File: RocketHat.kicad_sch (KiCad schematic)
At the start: 24 parts, among them J1 Screw_Terminal_01x02, J10 Raspberry_Pi_2_3, J2 Conn_01x06_Female, J3 Conn_01x06_Female, J4 Conn_01x07_Female, J5 Conn_01x06_Female, J6 Conn_01x04_Female, J7 Conn_01x10_Female, J9 Conn_01x10_Female, Q1 FQP27P06, U1 CAT24C128

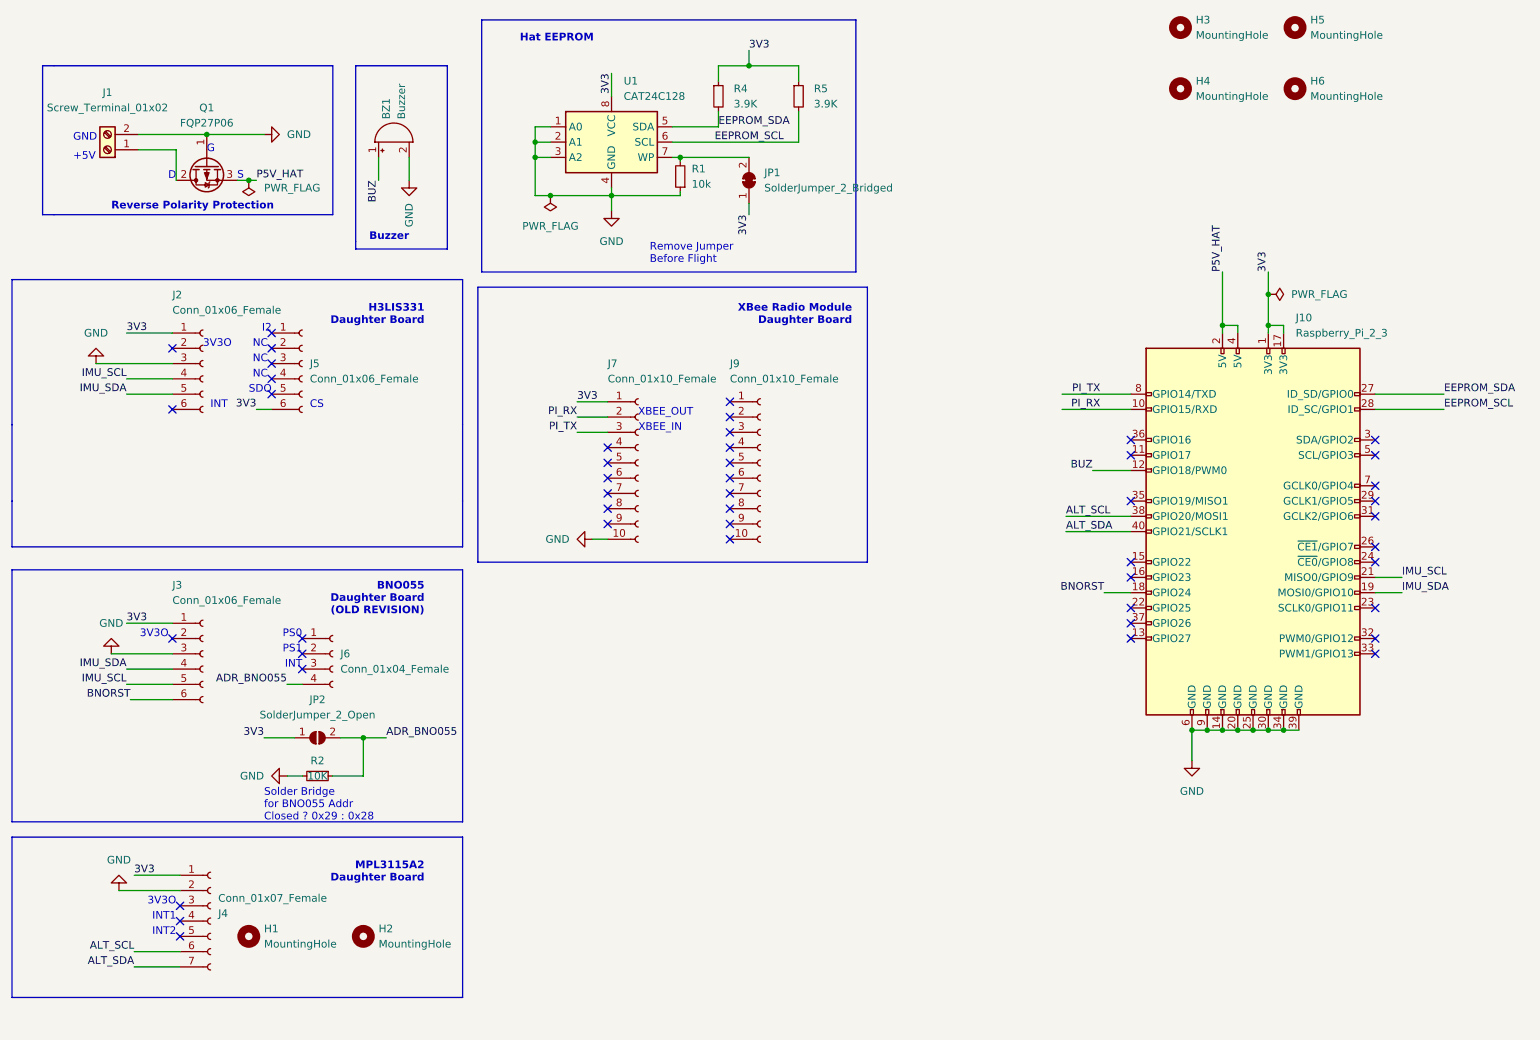
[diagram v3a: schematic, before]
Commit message: Added Mounting Holes for all sensors
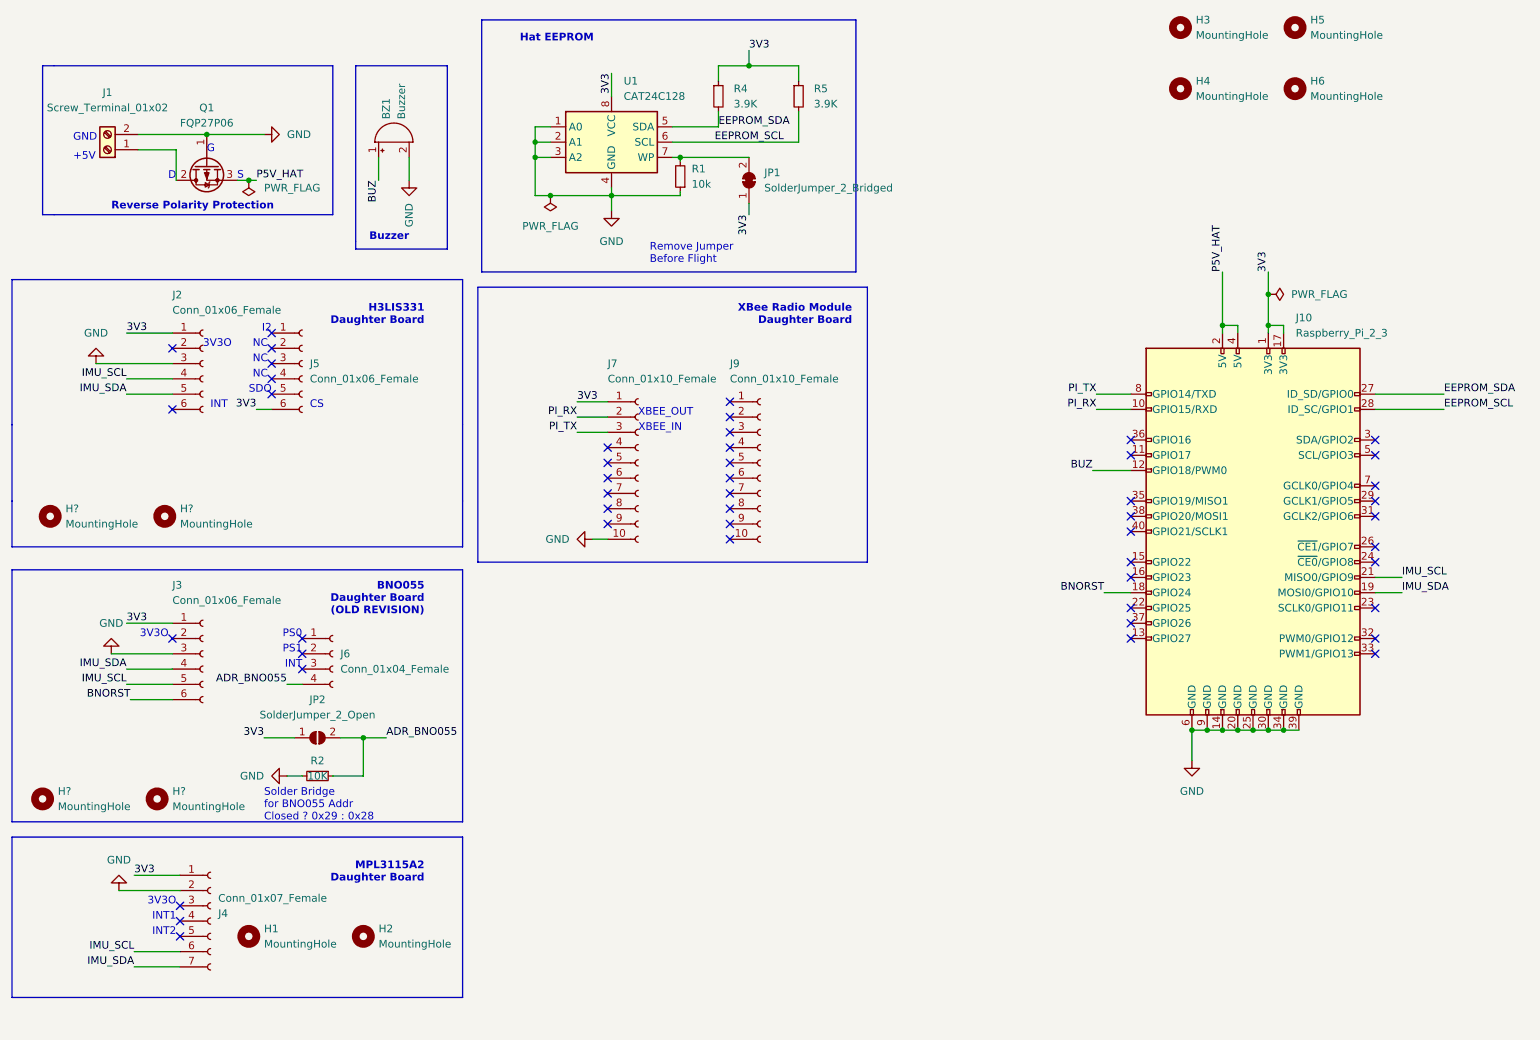
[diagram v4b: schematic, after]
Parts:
- added H? (x4): MountingHole, MountingHole:MountingHole_2.2mm_M2, symbol Mechanical:MountingHole
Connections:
- net IMU_SCL: now also J4.6 (Pin_6)
- net IMU_SDA: now also J4.7 (Pin_7)
- net ALT_SCL: no longer names the net of J10.38 (GPIO20/MOSI1)
- net ALT_SCL: no longer J4.6 (Pin_6)
- net ALT_SDA: no longer names the net of J10.40 (GPIO21/SCLK1)
- net ALT_SDA: no longer J4.7 (Pin_7)
- no-connect marks 48 -> 50
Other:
- company: (none) -> Rose-Hulman Rocketry Team
- title: (none) -> Rocket Hat PCB
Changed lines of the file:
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@@
 (kicad_sch (version 20211123) (generator eeschema)
   (paper "A4")
+  (title_block
+    (title "Rocket Hat PCB")
+    (date "2022-04-22")
+    (rev "1.1")
+    (company "Rose-Hulman Rocketry Team")
+    (comment 2 "https://creativecommons.org/licenses/by-sa/4.0/")
+    (comment 3 "License: CC BY-SA 4.0")
+    (comment 4 "Designed by Jacob Armstrong")
+  )
   (junction (at 155.575 26.67) (diameter 0) (color 0 0 0 0)
   )
@@
   (no_connect (at 152.4 105.41))
   (no_connect (at 132.08 95.25))
+  (no_connect (at 219.075 101.6))
   (no_connect (at 76.2 78.74))
   (no_connect (at 76.2 76.2))
@@
   (no_connect (at 152.4 97.79))
   (no_connect (at 152.4 85.09))
+  (no_connect (at 219.075 104.14))
   (no_connect (at 59.69 121.92))
   (no_connect (at 152.4 92.71))
@@
     (stroke (width 0) (type default) (color 0 0 0 0))
   )
+  (wire (pts (xy 213.36 83.82) (xy 219.075 83.82))
+    (stroke (width 0) (type default) (color 0 0 0 0))
+  )
   (polyline (pts (xy 173.355 19.05) (xy 173.355 60.96))
     (stroke (width 0) (type default) (color 0 0 0 0))
@@
     (stroke (width 0) (type default) (color 0 0 0 0))
   )
-  (wire (pts (xy 208.28 104.14) (xy 219.075 104.14))
-    (stroke (width 0) (type default) (color 0 0 0 0))
-  )
   (wire (pts (xy 259.715 114.3) (xy 264.16 114.3))
     (stroke (width 0) (type default) (color 0 0 0 0))
@@
     (stroke (width 0) (type default) (color 0 0 0 0))
   )
-  (wire (pts (xy 207.645 83.82) (xy 219.075 83.82))
-    (stroke (width 0) (type default) (color 0 0 0 0))
-  )
   (wire (pts (xy 142.875 39.37) (xy 163.83 39.37))
     (stroke (width 0) (type default) (color 0 0 0 0))
@@
     (stroke (width 0) (type default) (color 0 0 0 0))
   )
-  (wire (pts (xy 207.645 81.28) (xy 219.075 81.28))
-    (stroke (width 0) (type default) (color 0 0 0 0))
-  )
   (wire (pts (xy 87.63 138.43) (xy 91.44 138.43))
     (stroke (width 0) (type default) (color 0 0 0 0))
@@
     (stroke (width 0) (type default) (color 0 0 0 0))
   )
+  (wire (pts (xy 213.36 81.28) (xy 219.075 81.28))
+    (stroke (width 0) (type default) (color 0 0 0 0))
+  )
   (wire (pts (xy 259.715 81.28) (xy 271.145 81.28))
     (stroke (width 0) (type default) (color 0 0 0 0))
@@
   )
   (wire (pts (xy 120.015 41.91) (xy 122.555 41.91))
-    (stroke (width 0) (type default) (color 0 0 0 0))
-  )
-  (wire (pts (xy 208.28 101.6) (xy 219.075 101.6))
     (stroke (width 0) (type default) (color 0 0 0 0))
   )
@@
     (effects (font (size 1.27 1.27)) (justify left bottom))
   )
-  (label "ALT_SCL" (at 53.34 173.99 180)
+  (label "IMU_SCL" (at 53.34 173.99 180)
     (effects (font (size 1.27 1.27)) (justify right bottom))
   )
@@
     (effects (font (size 1.27 1.27)) (justify left bottom))
   )
-  (label "ALT_SCL" (at 208.28 101.6 0)
-    (effects (font (size 1.27 1.27)) (justify left bottom))
-  )
   (label "BUZ" (at 212.725 93.98 180)
     (effects (font (size 1.27 1.27)) (justify right bottom))
   )
-  (label "PI_RX" (at 213.995 83.82 180)
+  (label "PI_RX" (at 213.36 83.82 180)
     (effects (font (size 1.27 1.27)) (justify right bottom))
   )
@@
     (effects (font (size 1.27 1.27)) (justify left bottom))
   )
-  (label "PI_TX" (at 213.995 81.28 180)
+  (label "PI_TX" (at 213.36 81.28 180)
     (effects (font (size 1.27 1.27)) (justify right bottom))
   )
@@
     (effects (font (size 1.27 1.27)) (justify right bottom))
   )
-  (label "ALT_SDA" (at 53.34 176.53 180)
-    (effects (font (size 1.27 1.27)) (justify right bottom))
-  )
-  (label "ALT_SDA" (at 208.28 104.14 0)
-    (effects (font (size 1.27 1.27)) (justify left bottom))
+  (label "IMU_SDA" (at 53.34 176.53 180)
+    (effects (font (size 1.27 1.27)) (justify right bottom))
   )
   (symbol (lib_id "Jumper:SolderJumper_2_Open") (at 83.82 138.43 0) (unit 1)
@@
     (pin "1")
     (pin "2")
+  )
+  (symbol (lib_id "Mechanical:MountingHole") (at 39.37 101.6 0) (unit 1)
+    (in_bom yes) (on_board yes) (fields_autoplaced)
+    (property "Reference" "H?" (id 0) (at 41.91 100.3299 0)
+      (effects (font (size 1.27 1.27)) (justify left))
+    )
+    (property "Value" "MountingHole" (id 1) (at 41.91 102.8699 0)
+      (effects (font (size 1.27 1.27)) (justify left))
+    )
+    (property "Footprint" "MountingHole:MountingHole_2.2mm_M2" (id 2) (at 39.37 101.6 0)
+      (effects (font (size 1.27 1.27)) hide)
+    )
+    (property "Datasheet" "~" (id 3) (at 39.37 101.6 0)
+      (effects (font (size 1.27 1.27)) hide)
+    )
   )
   (symbol (lib_id "Connector:Raspberry_Pi_2_3") (at 239.395 104.14 0) (unit 1)
@@
     (pin "9")
   )
+  (symbol (lib_id "Mechanical:MountingHole") (at 58.42 101.6 0) (unit 1)
+    (in_bom yes) (on_board yes) (fields_autoplaced)
+    (property "Reference" "H?" (id 0) (at 60.96 100.3299 0)
+      (effects (font (size 1.27 1.27)) (justify left))
+    )
+    (property "Value" "MountingHole" (id 1) (at 60.96 102.8699 0)
+      (effects (font (size 1.27 1.27)) (justify left))
+    )
+    (property "Footprint" "MountingHole:MountingHole_2.2mm_M2" (id 2) (at 58.42 101.6 0)
+      (effects (font (size 1.27 1.27)) hide)
+    )
+    (property "Datasheet" "~" (id 3) (at 58.42 101.6 0)
+      (effects (font (size 1.27 1.27)) hide)
+    )
+  )
   (symbol (lib_id "Connector:Conn_01x06_Female") (at 64.77 124.46 0) (unit 1)
     (in_bom yes) (on_board yes)
@@
     )
   )
+  (symbol (lib_id "Mechanical:MountingHole") (at 38.1 148.59 0) (unit 1)
+    (in_bom yes) (on_board yes) (fields_autoplaced)
+    (property "Reference" "H?" (id 0) (at 40.64 147.3199 0)
+      (effects (font (size 1.27 1.27)) (justify left))
+    )
+    (property "Value" "MountingHole" (id 1) (at 40.64 149.8599 0)
+      (effects (font (size 1.27 1.27)) (justify left))
+    )
+    (property "Footprint" "MountingHole:MountingHole_2.2mm_M2" (id 2) (at 38.1 148.59 0)
+      (effects (font (size 1.27 1.27)) hide)
+    )
+    (property "Datasheet" "~" (id 3) (at 38.1 148.59 0)
+      (effects (font (size 1.27 1.27)) hide)
+    )
+  )
   (symbol (lib_id "power:GND") (at 49.53 124.46 180) (unit 1)
     (in_bom yes) (on_board yes) (fields_autoplaced)
@@
     (pin "1")
   )
+  (symbol (lib_id "Mechanical:MountingHole") (at 57.15 148.59 0) (unit 1)
+    (in_bom yes) (on_board yes) (fields_autoplaced)
+    (property "Reference" "H?" (id 0) (at 59.69 147.3199 0)
+      (effects (font (size 1.27 1.27)) (justify left))
+    )
+    (property "Value" "MountingHole" (id 1) (at 59.69 149.8599 0)
+      (effects (font (size 1.27 1.27)) (justify left))
+    )
+    (property "Footprint" "MountingHole:MountingHole_2.2mm_M2" (id 2) (at 57.15 148.59 0)
+      (effects (font (size 1.27 1.27)) hide)
+    )
+    (property "Datasheet" "~" (id 3) (at 57.15 148.59 0)
+      (effects (font (size 1.27 1.27)) hide)
+    )
+  )
   (symbol (lib_id "power:GND") (at 78.74 144.78 270) (unit 1)
     (in_bom yes) (on_board yes) (fields_autoplaced)
@@
       (reference "H6") (unit 1) (value "MountingHole") (footprint "MountingHole:MountingHole_2.7mm_M2.5")
     )
+    (path "/13969585-13f2-465b-9549-408e45124d57"
+      (reference "H?") (unit 1) (value "MountingHole") (footprint "MountingHole:MountingHole_2.2mm_M2")
+    )
+    (path "/1f72a00b-25f7-4dca-8312-516644df28d2"
+      (reference "H?") (unit 1) (value "MountingHole") (footprint "MountingHole:MountingHole_2.2mm_M2")
+    )
+    (path "/c8141d23-80b7-41ab-8d00-06dce93485de"
+      (reference "H?") (unit 1) (value "MountingHole") (footprint "MountingHole:MountingHole_2.2mm_M2")
+    )
+    (path "/e1438e2f-d85a-4663-b2b3-dbf709e33e71"
+      (reference "H?") (unit 1) (value "MountingHole") (footprint "MountingHole:MountingHole_2.2mm_M2")
+    )
     (path "/98240047-3dc2-4a0c-8573-518a35262738"

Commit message: Cleared Layout
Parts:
- BZ1: footprint Buzzer_Beeper:Buzzer_12x9.5RM7.6 -> Buzzer_Beeper:Buzzer_TDK_PS1240P02BT_D12.2mm_H6.5mm
- gave numbers to parts that had none: 4
- renumbered H6 to H10, H1 to H5, H2 to H6, H3 to H7, H4 to H8, H5 to H9, J5 to J3, J3 to J4, J6 to J5, J4 to J6, J9 to J8, J10 to J9, JP2 to JP1, JP1 to JP2, R2 to R1, R1 to R2, R4 to R3, R5 to R4
